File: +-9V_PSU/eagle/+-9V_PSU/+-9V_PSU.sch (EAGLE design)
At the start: 24 parts, among them IC1 7809TV, IC2 7909TV

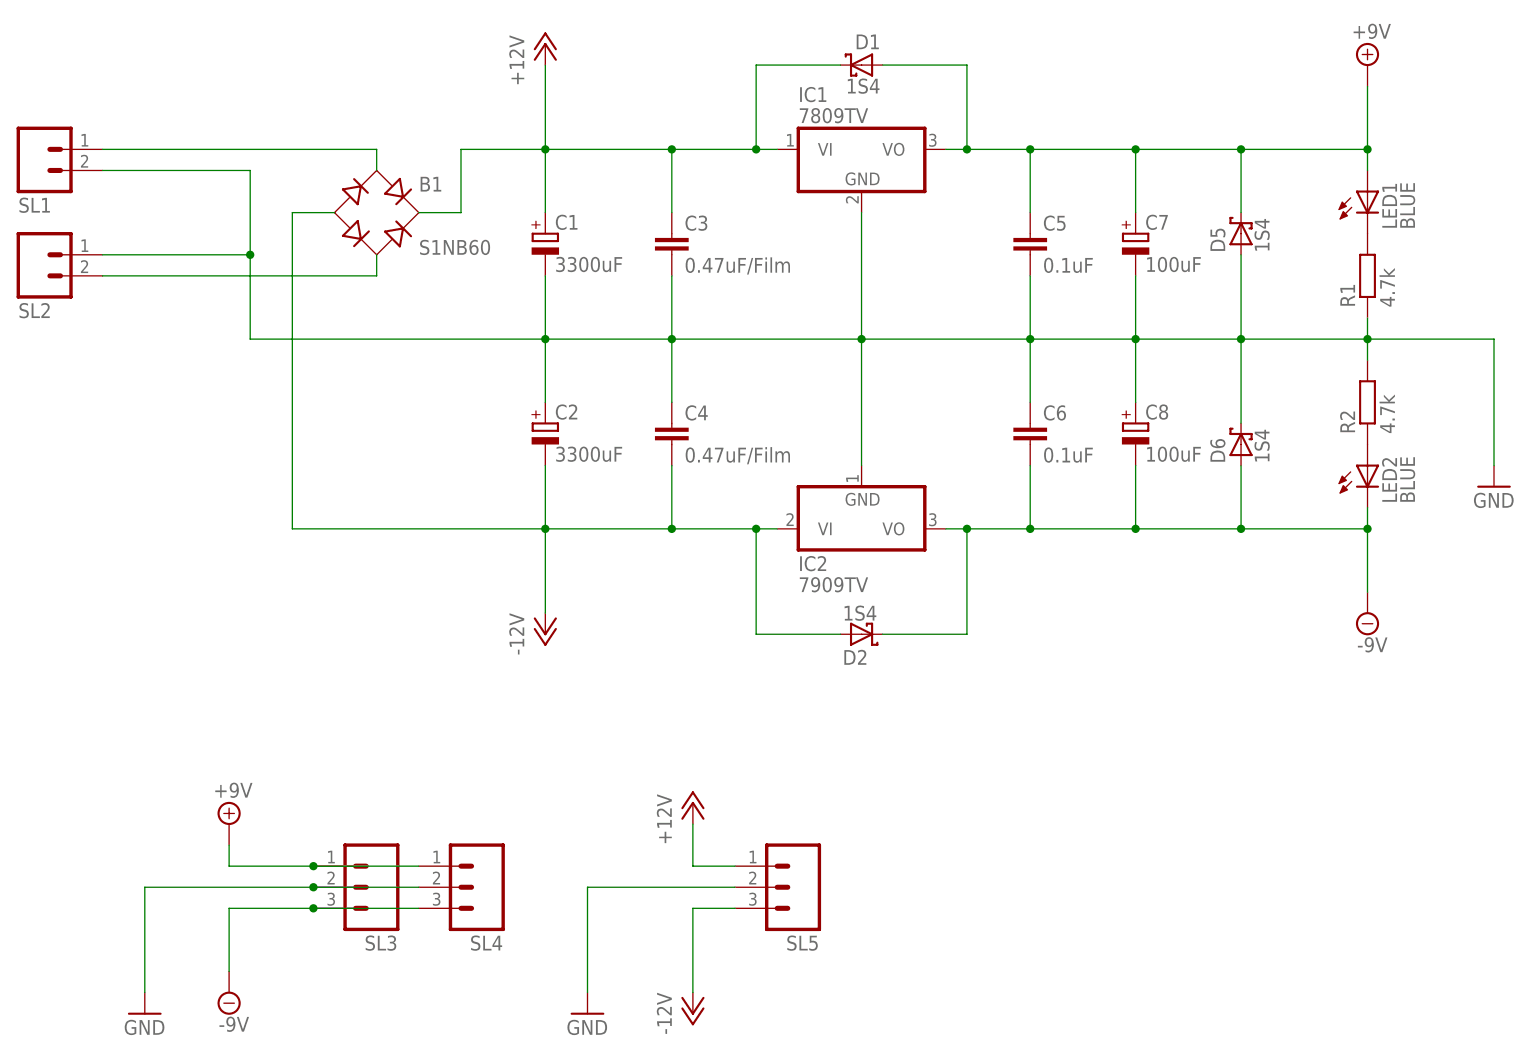
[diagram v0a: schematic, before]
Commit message: +-9V PSU Board design
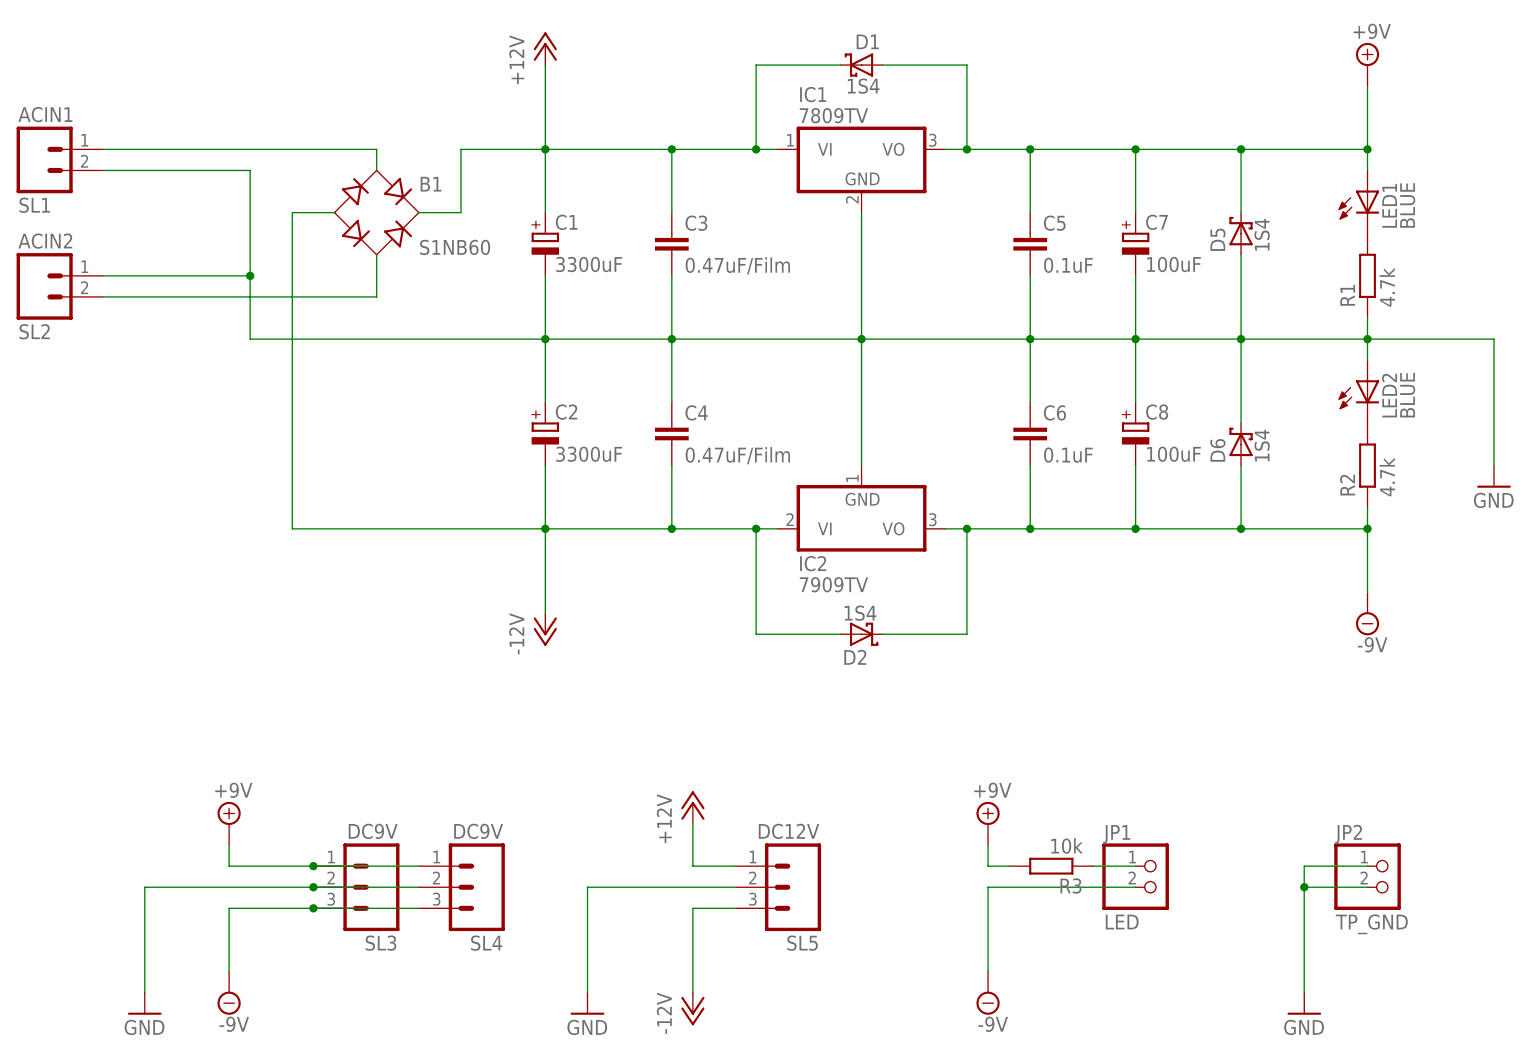
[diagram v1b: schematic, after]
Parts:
- added JP1: LED, pinhead:PINHD-1X2
- added JP2: TP_GND, pinhead:PINHD-1X2
- added R3: 10k, rcl:R-EU_0207/7
- C5, C6: device rcl:C-EU050-024X044 -> rcl:C-EU025-024X044
- SL1: value (none) -> ACIN1
- SL2: value (none) -> ACIN2
- SL3, SL4: value (none) -> DC9V
- SL5: value (none) -> DC12V
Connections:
- new net N$2: JP1.1, R3.1
- net +9V: now also R3.2
- net -9V: now also JP1.2, R2.1; no longer LED2.C
- net GND: now also JP2.1, JP2.2, LED2.A; no longer R2.2
- net N$1: now also LED2.C, R2.2; no longer LED2.A, R2.1
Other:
- moved on the sheet: LED2, R2, SL2
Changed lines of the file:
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@@
 <setting verticaltext="up"/>
 </settings>
-<grid distance="0.1" unitdist="inch" unit="inch" style="lines" multiple="1" display="yes" altdistance="0.01" altunitdist="inch" altunit="inch"/>
+<grid distance="0.1" unitdist="inch" unit="inch" style="lines" multiple="1" display="no" altdistance="0.01" altunitdist="inch" altunit="inch"/>
 <layers>
 <layer number="1" name="Top" color="4" fill="1" visible="no" active="no"/>
@@
 <part name="C3" library="rcl" deviceset="C-EU" device="050-045X075" value="0.47uF/Film"/>
 <part name="C4" library="rcl" deviceset="C-EU" device="050-045X075" value="0.47uF/Film"/>
-<part name="C5" library="rcl" deviceset="C-EU" device="050-024X044" value="0.1uF"/>
-<part name="C6" library="rcl" deviceset="C-EU" device="050-024X044" value="0.1uF"/>
+<part name="C5" library="rcl" deviceset="C-EU" device="025-024X044" value="0.1uF"/>
+<part name="C6" library="rcl" deviceset="C-EU" device="025-024X044" value="0.1uF"/>
 <part name="D2" library="diode" deviceset="SCHOTTKY-DIODE" device="DO35-7" value="1S4"/>
 <part name="C8" library="rcl" deviceset="CPOL-EU" device="SANYO_C6" value="100uF"/>
@@
 <part name="P-2" library="supply1" deviceset="-12V" device=""/>
 <part name="GND3" library="supply1" deviceset="GND" device=""/>
-<part name="SL3" library="con-amp-quick" deviceset="M03" device=""/>
-<part name="SL4" library="con-amp-quick" deviceset="M03" device=""/>
-<part name="SL5" library="con-amp-quick" deviceset="M03" device=""/>
-<part name="SL1" library="con-amp-quick" deviceset="M02" device=""/>
-<part name="SL2" library="con-amp-quick" deviceset="M02" device=""/>
+<part name="SL3" library="con-amp-quick" deviceset="M03" device="" value="DC9V"/>
+<part name="SL4" library="con-amp-quick" deviceset="M03" device="" value="DC9V"/>
+<part name="SL5" library="con-amp-quick" deviceset="M03" device="" value="DC12V"/>
+<part name="SL1" library="con-amp-quick" deviceset="M02" device="" value="ACIN1"/>
+<part name="SL2" library="con-amp-quick" deviceset="M02" device="" value="ACIN2"/>
+<part name="SUPPLY5" library="supply2" deviceset="+9V" device=""/>
+<part name="SUPPLY6" library="supply2" deviceset="-9V" device=""/>
+<part name="R3" library="rcl" deviceset="R-EU_" device="0207/7" value="10k"/>
+<part name="JP1" library="pinhead" deviceset="PINHD-1X2" device="" value="LED"/>
+<part name="JP2" library="pinhead" deviceset="PINHD-1X2" device="" value="TP_GND"/>
+<part name="GND4" library="supply1" deviceset="GND" device=""/>
 </parts>
 <sheets>
@@
 <instance part="C8" gate="G$1" x="167.64" y="111.76"/>
 <instance part="R1" gate="G$1" x="195.58" y="129.54" rot="R90"/>
-<instance part="R2" gate="G$1" x="195.58" y="114.3" rot="R90"/>
+<instance part="R2" gate="G$1" x="195.58" y="106.68" rot="R90"/>
 <instance part="LED1" gate="G$1" x="195.58" y="139.7"/>
-<instance part="LED2" gate="G$1" x="195.58" y="106.68"/>
+<instance part="LED2" gate="G$1" x="195.58" y="116.84"/>
 <instance part="SUPPLY1" gate="G$1" x="195.58" y="154.94"/>
 <instance part="SUPPLY2" gate="G$1" x="195.58" y="88.9"/>
@@
 <instance part="SL5" gate="G$1" x="127" y="55.88" rot="R180"/>
 <instance part="SL1" gate="G$1" x="35.56" y="144.78" rot="MR180"/>
-<instance part="SL2" gate="G$1" x="35.56" y="132.08" rot="MR180"/>
+<instance part="SL2" gate="G$1" x="35.56" y="129.54" rot="MR180"/>
+<instance part="SUPPLY5" gate="G$1" x="149.86" y="63.5"/>
+<instance part="SUPPLY6" gate="G$1" x="149.86" y="43.18"/>
+<instance part="R3" gate="G$1" x="157.48" y="58.42" rot="R180"/>
+<instance part="JP1" gate="G$1" x="170.18" y="55.88"/>
+<instance part="JP2" gate="G$1" x="198.12" y="55.88"/>
+<instance part="GND4" gate="1" x="187.96" y="40.64"/>
 </instances>
 <busses>
@@
 <pinref part="D5" gate="G$1" pin="A"/>
 <pinref part="D6" gate="G$1" pin="C"/>
-<pinref part="R2" gate="G$1" pin="2"/>
-<wire x1="195.58" y1="119.38" x2="195.58" y2="121.92" width="0.1524" layer="91"/>
 <junction x="195.58" y="121.92"/>
 <pinref part="R1" gate="G$1" pin="1"/>
@@
 <pinref part="C2" gate="G$1" pin="+"/>
 <wire x1="96.52" y1="121.92" x2="96.52" y2="114.3" width="0.1524" layer="91"/>
-<wire x1="60.96" y1="142.24" x2="60.96" y2="132.08" width="0.1524" layer="91"/>
-<wire x1="60.96" y1="132.08" x2="60.96" y2="121.92" width="0.1524" layer="91"/>
+<wire x1="60.96" y1="142.24" x2="60.96" y2="129.54" width="0.1524" layer="91"/>
+<wire x1="60.96" y1="129.54" x2="60.96" y2="121.92" width="0.1524" layer="91"/>
 <wire x1="60.96" y1="121.92" x2="96.52" y2="121.92" width="0.1524" layer="91"/>
 <pinref part="SL2" gate="G$1" pin="1"/>
-<wire x1="43.18" y1="132.08" x2="60.96" y2="132.08" width="0.1524" layer="91"/>
-<junction x="60.96" y="132.08"/>
+<wire x1="43.18" y1="129.54" x2="60.96" y2="129.54" width="0.1524" layer="91"/>
+<junction x="60.96" y="129.54"/>
 <pinref part="SL1" gate="G$1" pin="2"/>
 <wire x1="60.96" y1="142.24" x2="43.18" y2="142.24" width="0.1524" layer="91"/>
+<pinref part="LED2" gate="G$1" pin="A"/>
+<wire x1="195.58" y1="119.38" x2="195.58" y2="121.92" width="0.1524" layer="91"/>
 </segment>
 <segment>
@@
 <wire x1="101.6" y1="55.88" x2="119.38" y2="55.88" width="0.1524" layer="91"/>
 </segment>
+<segment>
+<pinref part="JP2" gate="G$1" pin="1"/>
+<pinref part="GND4" gate="1" pin="GND"/>
+<wire x1="195.58" y1="58.42" x2="187.96" y2="58.42" width="0.1524" layer="91"/>
+<wire x1="187.96" y1="58.42" x2="187.96" y2="55.88" width="0.1524" layer="91"/>
+<pinref part="JP2" gate="G$1" pin="2"/>
+<wire x1="187.96" y1="55.88" x2="187.96" y2="43.18" width="0.1524" layer="91"/>
+<wire x1="195.58" y1="55.88" x2="187.96" y2="55.88" width="0.1524" layer="91"/>
+<junction x="187.96" y="55.88"/>
+</segment>
 </net>
 <net name="-9V" class="0">
@@
 <pinref part="IC2" gate="G$1" pin="VO"/>
 <wire x1="144.78" y1="99.06" x2="147.32" y2="99.06" width="0.1524" layer="91"/>
-<pinref part="LED2" gate="G$1" pin="C"/>
 <wire x1="147.32" y1="99.06" x2="154.94" y2="99.06" width="0.1524" layer="91"/>
 <wire x1="154.94" y1="99.06" x2="167.64" y2="99.06" width="0.1524" layer="91"/>
 <wire x1="167.64" y1="99.06" x2="180.34" y2="99.06" width="0.1524" layer="91"/>
 <wire x1="180.34" y1="99.06" x2="195.58" y2="99.06" width="0.1524" layer="91"/>
-<wire x1="195.58" y1="99.06" x2="195.58" y2="101.6" width="0.1524" layer="91"/>
 <junction x="180.34" y="99.06"/>
 <pinref part="C6" gate="G$1" pin="2"/>
@@
 <wire x1="180.34" y1="99.06" x2="180.34" y2="106.68" width="0.1524" layer="91"/>
 <wire x1="195.58" y1="91.44" x2="195.58" y2="99.06" width="0.1524" layer="91"/>
-<junction x="195.58" y="99.06"/>
 <pinref part="D6" gate="G$1" pin="A"/>
 <pinref part="D2" gate="G$1" pin="C"/>
 <pinref part="SUPPLY2" gate="G$1" pin="-9V"/>
+<pinref part="R2" gate="G$1" pin="1"/>
+<wire x1="195.58" y1="101.6" x2="195.58" y2="99.06" width="0.1524" layer="91"/>
+<junction x="195.58" y="99.06"/>
 </segment>
 <segment>
@@
 <wire x1="81.28" y1="53.34" x2="68.58" y2="53.34" width="0.1524" layer="91"/>
 <junction x="68.58" y="53.34"/>
+</segment>
+<segment>
+<pinref part="JP1" gate="G$1" pin="2"/>
+<wire x1="167.64" y1="55.88" x2="149.86" y2="55.88" width="0.1524" layer="91"/>
+<wire x1="149.86" y1="55.88" x2="149.86" y2="45.72" width="0.1524" layer="91"/>
+<pinref part="SUPPLY6" gate="G$1" pin="-9V"/>
 </segment>
 </net>
@@
 <junction x="68.58" y="58.42"/>
 </segment>
-</net>
-<net name="N$1" class="0">
-<segment>
-<pinref part="LED2" gate="G$1" pin="A"/>
-<pinref part="R2" gate="G$1" pin="1"/>
+<segment>
+<pinref part="SUPPLY5" gate="G$1" pin="+9V"/>
+<wire x1="149.86" y1="60.96" x2="149.86" y2="58.42" width="0.1524" layer="91"/>
+<pinref part="R3" gate="G$1" pin="2"/>
+<wire x1="149.86" y1="58.42" x2="152.4" y2="58.42" width="0.1524" layer="91"/>
 </segment>
 </net>
@@
 <net name="N$6" class="0">
 <segment>
-<wire x1="43.18" y1="129.54" x2="76.2" y2="129.54" width="0.1524" layer="91"/>
+<wire x1="43.18" y1="127" x2="76.2" y2="127" width="0.1524" layer="91"/>
 <pinref part="B1" gate="1" pin="AC2"/>
-<wire x1="76.2" y1="129.54" x2="76.2" y2="132.08" width="0.1524" layer="91"/>
+<wire x1="76.2" y1="127" x2="76.2" y2="132.08" width="0.1524" layer="91"/>
 <pinref part="SL2" gate="G$1" pin="2"/>
 </segment>
@@
 </segment>
 </net>
+<net name="N$1" class="0">
+<segment>
+<pinref part="LED2" gate="G$1" pin="C"/>
+<pinref part="R2" gate="G$1" pin="2"/>
+</segment>
+</net>
+<net name="N$2" class="0">
+<segment>
+<pinref part="R3" gate="G$1" pin="1"/>
+<pinref part="JP1" gate="G$1" pin="1"/>
+<wire x1="162.56" y1="58.42" x2="167.64" y2="58.42" width="0.1524" layer="91"/>
+</segment>
+</net>
